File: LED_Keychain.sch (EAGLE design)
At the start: 0 parts

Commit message: Added key switches
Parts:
- added U$2: KEYSWITCH-PLAIN-MX-1U, Keyboard:KEYSWITCH-PLAIN-MX-1U
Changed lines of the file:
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@@
 <layer number="48" name="Document" color="7" fill="1" visible="no" active="no"/>
 <layer number="49" name="Reference" color="7" fill="1" visible="no" active="no"/>
+<layer number="50" name="dxf" color="7" fill="1" visible="no" active="no"/>
 <layer number="51" name="tDocu" color="7" fill="1" visible="no" active="no"/>
 <layer number="52" name="bDocu" color="7" fill="1" visible="no" active="no"/>
+<layer number="53" name="tGND_GNDA" color="7" fill="9" visible="no" active="no"/>
+<layer number="54" name="bGND_GNDA" color="1" fill="9" visible="no" active="no"/>
+<layer number="56" name="wert" color="7" fill="1" visible="no" active="no"/>
+<layer number="57" name="tCAD" color="7" fill="1" visible="no" active="no"/>
+<layer number="59" name="tCarbon" color="7" fill="1" visible="no" active="no"/>
+<layer number="60" name="bCarbon" color="7" fill="1" visible="no" active="no"/>
 <layer number="88" name="SimResults" color="9" fill="1" visible="yes" active="yes"/>
 <layer number="89" name="SimProbes" color="9" fill="1" visible="yes" active="yes"/>
@@
 <layer number="97" name="Info" color="7" fill="1" visible="yes" active="yes"/>
 <layer number="98" name="Guide" color="6" fill="1" visible="yes" active="yes"/>
+<layer number="99" name="SpiceOrder" color="7" fill="1" visible="yes" active="yes"/>
+<layer number="100" name="Muster" color="7" fill="1" visible="no" active="no"/>
+<layer number="101" name="Patch_Top" color="12" fill="4" visible="no" active="no"/>
+<layer number="102" name="Vscore" color="7" fill="1" visible="no" active="no"/>
+<layer number="103" name="tMap" color="7" fill="1" visible="no" active="no"/>
+<layer number="104" name="Name" color="7" fill="1" visible="no" active="no"/>
+<layer number="105" name="tPlate" color="7" fill="1" visible="no" active="no"/>
+<layer number="106" name="bPlate" color="7" fill="1" visible="no" active="no"/>
+<layer number="107" name="Crop" color="7" fill="1" visible="no" active="no"/>
+<layer number="108" name="fp8" color="7" fill="1" visible="no" active="no"/>
+<layer number="109" name="fp9" color="7" fill="1" visible="no" active="no"/>
+<layer number="110" name="110" color="7" fill="1" visible="no" active="no"/>
+<layer number="111" name="111" color="7" fill="1" visible="no" active="no"/>
+<layer number="112" name="tSilk" color="7" fill="1" visible="no" active="no"/>
+<layer number="113" name="IDFDebug" color="7" fill="1" visible="no" active="yes"/>
+<layer number="114" name="FRNTMAAT1" color="7" fill="1" visible="yes" active="yes"/>
+<layer number="115" name="FRNTMAAT2" color="7" fill="1" visible="yes" active="yes"/>
+<layer number="116" name="Patch_BOT" color="9" fill="4" visible="no" active="no"/>
+<layer number="117" name="BACKMAAT1" color="7" fill="1" visible="yes" active="yes"/>
+<layer number="118" name="Rect_Pads" color="7" fill="1" visible="no" active="no"/>
+<layer number="119" name="KAP_TEKEN" color="7" fill="1" visible="yes" active="yes"/>
+<layer number="120" name="KAP_MAAT1" color="7" fill="1" visible="yes" active="yes"/>
+<layer number="121" name="_tsilk" color="7" fill="1" visible="no" active="no"/>
+<layer number="122" name="_bsilk" color="7" fill="1" visible="no" active="no"/>
+<layer number="123" name="tTestmark" color="7" fill="1" visible="no" active="no"/>
+<layer number="124" name="bTestmark" color="7" fill="1" visible="no" active="no"/>
+<layer number="125" name="_tNames" color="7" fill="1" visible="no" active="no"/>
+<layer number="126" name="_bNames" color="7" fill="1" visible="no" active="no"/>
+<layer number="127" name="_tValues" color="7" fill="1" visible="no" active="no"/>
+<layer number="128" name="_bValues" color="7" fill="1" visible="no" active="no"/>
+<layer number="129" name="top_silk" color="7" fill="1" visible="yes" active="yes"/>
+<layer number="130" name="SMDSTROOK" color="7" fill="1" visible="yes" active="yes"/>
+<layer number="131" name="tAdjust" color="7" fill="1" visible="no" active="no"/>
+<layer number="132" name="bAdjust" color="7" fill="1" visible="no" active="no"/>
+<layer number="133" name="bottom_silk" color="7" fill="1" visible="yes" active="yes"/>
+<layer number="144" name="DrillLegend" color="7" fill="1" visible="no" active="no"/>
+<layer number="150" name="Notes" color="7" fill="1" visible="no" active="yes"/>
+<layer number="151" name="HeatSink" color="14" fill="1" visible="no" active="no"/>
+<layer number="152" name="_bDocu" color="7" fill="1" visible="no" active="no"/>
+<layer number="153" name="FabDoc1" color="6" fill="1" visible="no" active="no"/>
+<layer number="154" name="FabDoc2" color="2" fill="1" visible="no" active="no"/>
+<layer number="155" name="FabDoc3" color="7" fill="15" visible="no" active="no"/>
+<layer number="199" name="Contour" color="7" fill="1" visible="no" active="no"/>
+<layer number="200" name="200bmp" color="1" fill="10" visible="no" active="no"/>
+<layer number="201" name="201bmp" color="2" fill="1" visible="no" active="no"/>
+<layer number="202" name="202bmp" color="3" fill="1" visible="no" active="no"/>
+<layer number="203" name="203bmp" color="4" fill="10" visible="no" active="no"/>
+<layer number="204" name="204bmp" color="5" fill="10" visible="no" active="no"/>
+<layer number="205" name="205bmp" color="6" fill="10" visible="no" active="no"/>
+<layer number="206" name="206bmp" color="7" fill="10" visible="no" active="no"/>
+<layer number="207" name="207bmp" color="15" fill="10" visible="no" active="no"/>
+<layer number="208" name="208bmp" color="9" fill="10" visible="no" active="no"/>
+<layer number="209" name="209bmp" color="7" fill="1" visible="no" active="no"/>
+<layer number="210" name="210bmp" color="7" fill="1" visible="no" active="no"/>
+<layer number="211" name="211bmp" color="7" fill="1" visible="no" active="no"/>
+<layer number="212" name="212bmp" color="7" fill="1" visible="no" active="no"/>
+<layer number="213" name="213bmp" color="7" fill="1" visible="no" active="no"/>
+<layer number="214" name="214bmp" color="7" fill="1" visible="no" active="no"/>
+<layer number="215" name="215bmp" color="7" fill="1" visible="no" active="no"/>
+<layer number="216" name="216bmp" color="7" fill="1" visible="no" active="no"/>
+<layer number="217" name="217bmp" color="18" fill="1" visible="no" active="no"/>
+<layer number="218" name="218bmp" color="19" fill="1" visible="no" active="no"/>
+<layer number="219" name="219bmp" color="20" fill="1" visible="no" active="no"/>
+<layer number="220" name="220bmp" color="21" fill="1" visible="no" active="no"/>
+<layer number="221" name="221bmp" color="22" fill="1" visible="no" active="no"/>
+<layer number="222" name="222bmp" color="23" fill="1" visible="no" active="no"/>
+<layer number="223" name="223bmp" color="24" fill="1" visible="no" active="no"/>
+<layer number="224" name="224bmp" color="25" fill="1" visible="no" active="no"/>
+<layer number="225" name="225bmp" color="7" fill="1" visible="no" active="yes"/>
+<layer number="226" name="226bmp" color="7" fill="1" visible="no" active="yes"/>
+<layer number="227" name="227bmp" color="7" fill="1" visible="no" active="yes"/>
+<layer number="228" name="228bmp" color="7" fill="1" visible="no" active="yes"/>
+<layer number="229" name="229bmp" color="7" fill="1" visible="yes" active="yes"/>
+<layer number="230" name="230bmp" color="7" fill="1" visible="no" active="yes"/>
+<layer number="231" name="Eagle3D_PG1" color="7" fill="1" visible="yes" active="yes"/>
+<layer number="232" name="Eagle3D_PG2" color="7" fill="1" visible="yes" active="yes"/>
+<layer number="233" name="Eagle3D_PG3" color="7" fill="1" visible="yes" active="yes"/>
+<layer number="248" name="Housing" color="7" fill="1" visible="no" active="no"/>
+<layer number="249" name="Edge" color="7" fill="1" visible="no" active="no"/>
+<layer number="250" name="Descript" color="3" fill="1" visible="no" active="no"/>
+<layer number="251" name="SMDround" color="12" fill="11" visible="no" active="no"/>
+<layer number="254" name="OrgLBR" color="13" fill="1" visible="no" active="no"/>
+<layer number="255" name="Accent" color="7" fill="1" visible="yes" active="yes"/>
 </layers>
 <schematic xreflabel="%F%N/%S.%C%R" xrefpart="/%S.%C%R">
@@
 <parts>
 <part name="FRAME1" library="frames" library_urn="urn:adsk.eagle:library:229" deviceset="FRAME_A_L" device=""/>
+<part name="U$2" library="Keyboard" deviceset="KEYSWITCH-PLAIN" device="-MX-1U"/>
 </parts>
 <sheets>
@@
 <attribute name="DRAWING_NAME" x="190.5" y="19.05" size="2.54" layer="94"/>
 </instance>
+<instance part="U$2" gate="G$1" x="66.04" y="111.76" smashed="yes">
+<attribute name="NAME" x="59.23" y="117.078" size="1" layer="95"/>
+</instance>
 </instances>

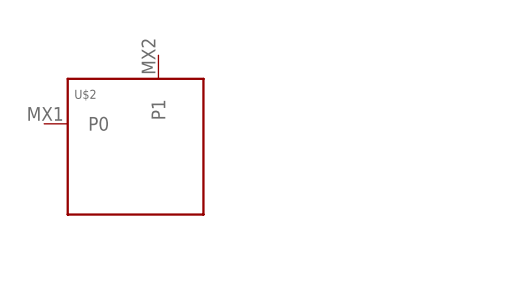
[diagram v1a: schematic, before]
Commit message: Added Keystone3035 in LED_Keychain_lib.lbr.
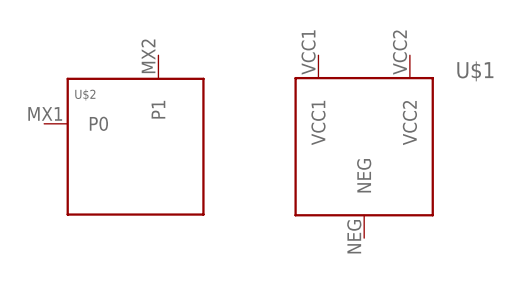
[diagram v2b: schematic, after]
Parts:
- added U$1: KEYSTONE3035, LED_Keychain_lib:KEYSTONE3035
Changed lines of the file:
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@@
 <part name="FRAME1" library="frames" library_urn="urn:adsk.eagle:library:229" deviceset="FRAME_A_L" device=""/>
 <part name="U$2" library="Keyboard" deviceset="KEYSWITCH-PLAIN" device="-MX-1U"/>
+<part name="U$1" library="LED_Keychain_lib" deviceset="KEYSTONE3035" device=""/>
 </parts>
 <sheets>
@@
 <attribute name="NAME" x="59.23" y="117.078" size="1" layer="95"/>
 </instance>
+<instance part="U$1" gate="G$1" x="91.44" y="111.76" smashed="yes">
+<attribute name="NAME" x="101.6" y="119.38" size="1.778" layer="95"/>
+</instance>
 </instances>

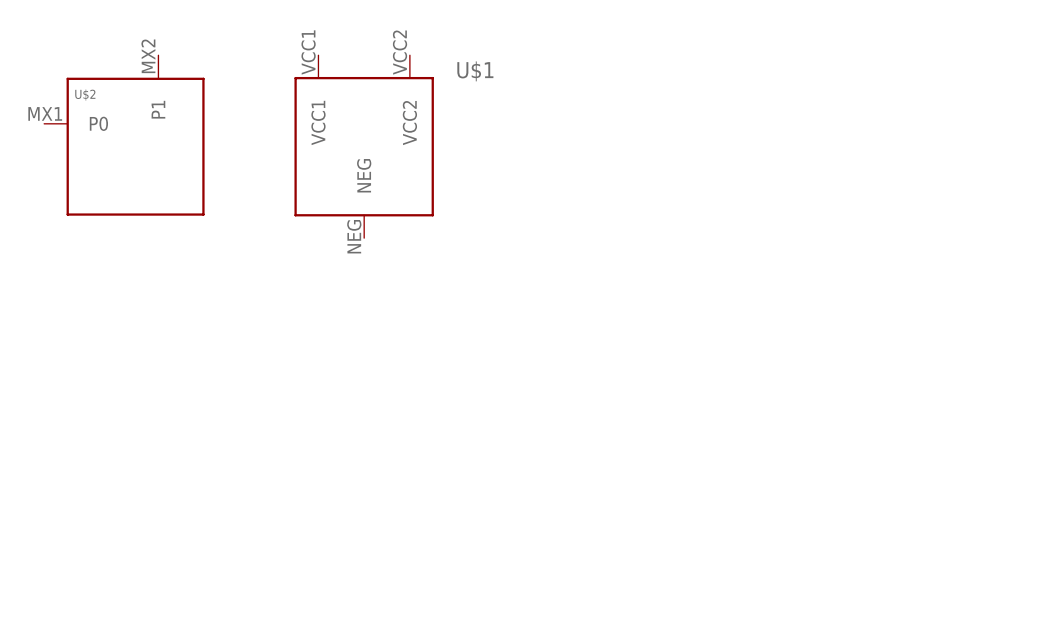
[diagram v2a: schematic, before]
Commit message: Layed out the board and finished the schematic
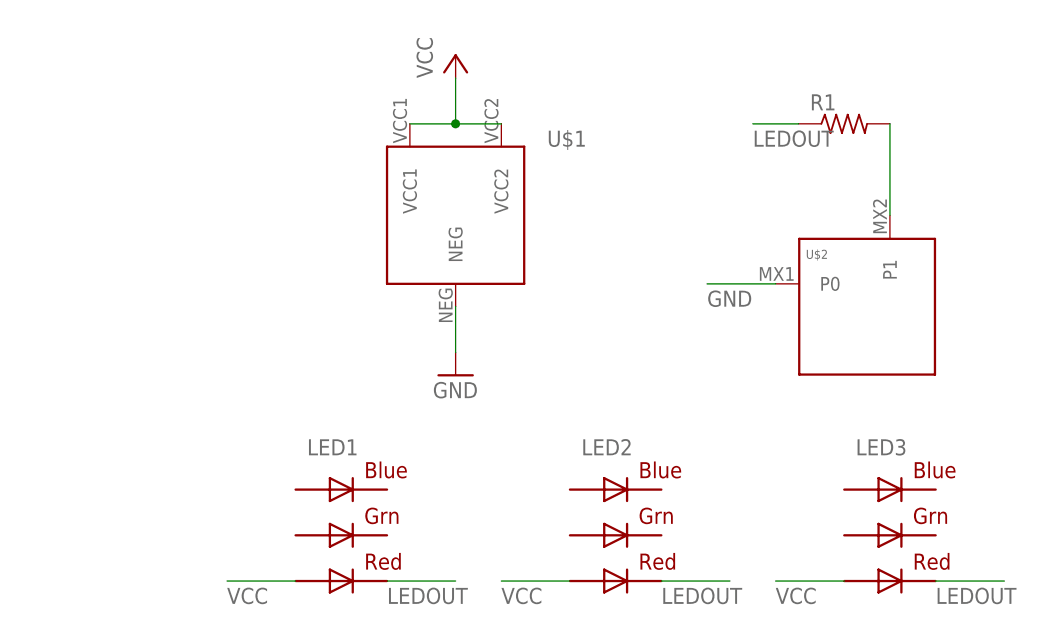
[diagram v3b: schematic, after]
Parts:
- added LED1, LED2, LED3: RGBLED5050, adafruit:RGBLED5050
- added R1: (no value), adafruit:R-US_R0603
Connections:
- new net GND: U$1.NEG, U$2.P0
- new net LEDOUT: LED1.RED_C, LED2.RED_C, LED3.RED_C, R1.1
- new net N$4: R1.2, U$2.P1
- new net VCC: LED1.RED_A, LED2.RED_A, LED3.RED_A, U$1.VCC1, U$1.VCC2
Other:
- moved on the sheet: U$1, U$2
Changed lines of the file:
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@@
 <part name="U$2" library="Keyboard" deviceset="KEYSWITCH-PLAIN" device="-MX-1U"/>
 <part name="U$1" library="LED_Keychain_lib" deviceset="KEYSTONE3035" device=""/>
+<part name="LED1" library="adafruit" deviceset="RGBLED" device="5050"/>
+<part name="R1" library="adafruit" deviceset="R-US_" device="R0603"/>
+<part name="GND1" library="supply1" library_urn="urn:adsk.eagle:library:371" deviceset="GND" device=""/>
+<part name="P+1" library="supply1" library_urn="urn:adsk.eagle:library:371" deviceset="VCC" device=""/>
+<part name="LED2" library="adafruit" deviceset="RGBLED" device="5050"/>
+<part name="LED3" library="adafruit" deviceset="RGBLED" device="5050"/>
 </parts>
 <sheets>
@@
 <attribute name="DRAWING_NAME" x="190.5" y="19.05" size="2.54" layer="94"/>
 </instance>
-<instance part="U$2" gate="G$1" x="66.04" y="111.76" smashed="yes">
-<attribute name="NAME" x="59.23" y="117.078" size="1" layer="95"/>
+<instance part="U$2" gate="G$1" x="147.32" y="93.98" smashed="yes">
+<attribute name="NAME" x="140.51" y="99.298" size="1" layer="95"/>
 </instance>
-<instance part="U$1" gate="G$1" x="91.44" y="111.76" smashed="yes">
-<attribute name="NAME" x="101.6" y="119.38" size="1.778" layer="95"/>
+<instance part="U$1" gate="G$1" x="101.6" y="104.14" smashed="yes">
+<attribute name="NAME" x="111.76" y="111.76" size="1.778" layer="95"/>
+</instance>
+<instance part="LED1" gate="G$1" x="88.9" y="68.58" smashed="yes">
+<attribute name="NAME" x="85.09" y="77.47" size="1.778" layer="95"/>
+</instance>
+<instance part="R1" gate="G$1" x="144.78" y="114.3" smashed="yes">
+<attribute name="NAME" x="140.97" y="115.7986" size="1.778" layer="95"/>
+<attribute name="VALUE" x="140.97" y="110.998" size="1.778" layer="96"/>
+</instance>
+<instance part="GND1" gate="1" x="101.6" y="86.36" smashed="yes">
+<attribute name="VALUE" x="99.06" y="83.82" size="1.778" layer="96"/>
+</instance>
+<instance part="P+1" gate="VCC" x="101.6" y="121.92" smashed="yes">
+<attribute name="VALUE" x="99.06" y="119.38" size="1.778" layer="96" rot="R90"/>
+</instance>
+<instance part="LED2" gate="G$1" x="119.38" y="68.58" smashed="yes">
+<attribute name="NAME" x="115.57" y="77.47" size="1.778" layer="95"/>
+</instance>
+<instance part="LED3" gate="G$1" x="149.86" y="68.58" smashed="yes">
+<attribute name="NAME" x="146.05" y="77.47" size="1.778" layer="95"/>
 </instance>
 </instances>
@@
 </busses>
 <nets>
+<net name="GND" class="0">
+<segment>
+<pinref part="U$1" gate="G$1" pin="NEG"/>
+<wire x1="101.6" y1="88.9" x2="101.6" y2="93.98" width="0.1524" layer="91"/>
+<pinref part="GND1" gate="1" pin="GND"/>
+</segment>
+<segment>
+<pinref part="U$2" gate="G$1" pin="P0"/>
+<wire x1="137.16" y1="96.52" x2="129.54" y2="96.52" width="0.1524" layer="91"/>
+<label x="129.54" y="93.98" size="1.778" layer="95"/>
+</segment>
+</net>
+<net name="N$4" class="0">
+<segment>
+<pinref part="R1" gate="G$1" pin="2"/>
+<pinref part="U$2" gate="G$1" pin="P1"/>
+<wire x1="149.86" y1="114.3" x2="149.86" y2="104.14" width="0.1524" layer="91"/>
+</segment>
+</net>
+<net name="VCC" class="0">
+<segment>
+<pinref part="U$1" gate="G$1" pin="VCC1"/>
+<pinref part="U$1" gate="G$1" pin="VCC2"/>
+<wire x1="96.52" y1="114.3" x2="101.6" y2="114.3" width="0.1524" layer="91"/>
+<pinref part="P+1" gate="VCC" pin="VCC"/>
+<wire x1="101.6" y1="114.3" x2="106.68" y2="114.3" width="0.1524" layer="91"/>
+<wire x1="101.6" y1="119.38" x2="101.6" y2="114.3" width="0.1524" layer="91"/>
+<junction x="101.6" y="114.3"/>
+</segment>
+<segment>
+<pinref part="LED1" gate="G$1" pin="RED_A"/>
+<wire x1="83.82" y1="63.5" x2="76.2" y2="63.5" width="0.1524" layer="91"/>
+<label x="76.2" y="60.96" size="1.778" layer="95"/>
+</segment>
+<segment>
+<pinref part="LED2" gate="G$1" pin="RED_A"/>
+<wire x1="114.3" y1="63.5" x2="106.68" y2="63.5" width="0.1524" layer="91"/>
+<label x="106.68" y="60.96" size="1.778" layer="95"/>
+</segment>
+<segment>
+<pinref part="LED3" gate="G$1" pin="RED_A"/>
+<wire x1="144.78" y1="63.5" x2="137.16" y2="63.5" width="0.1524" layer="91"/>
+<label x="137.16" y="60.96" size="1.778" layer="95"/>
+</segment>
+</net>
+<net name="LEDOUT" class="0">
+<segment>
+<pinref part="R1" gate="G$1" pin="1"/>
+<wire x1="139.7" y1="114.3" x2="134.62" y2="114.3" width="0.1524" layer="91"/>
+<label x="134.62" y="111.76" size="1.778" layer="95"/>
+</segment>
+<segment>
+<pinref part="LED1" gate="G$1" pin="RED_C"/>
+<wire x1="93.98" y1="63.5" x2="101.6" y2="63.5" width="0.1524" layer="91"/>
+<label x="93.98" y="60.96" size="1.778" layer="95"/>
+</segment>
+<segment>
+<pinref part="LED2" gate="G$1" pin="RED_C"/>
+<wire x1="124.46" y1="63.5" x2="132.08" y2="63.5" width="0.1524" layer="91"/>
+<label x="124.46" y="60.96" size="1.778" layer="95"/>
+</segment>
+<segment>
+<pinref part="LED3" gate="G$1" pin="RED_C"/>
+<wire x1="154.94" y1="63.5" x2="162.56" y2="63.5" width="0.1524" layer="91"/>
+<label x="154.94" y="60.96" size="1.778" layer="95"/>
+</segment>
+</net>
 </nets>
 </sheet>
